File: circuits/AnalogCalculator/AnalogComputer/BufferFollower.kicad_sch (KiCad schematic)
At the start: 1 part, among them U7 LM324

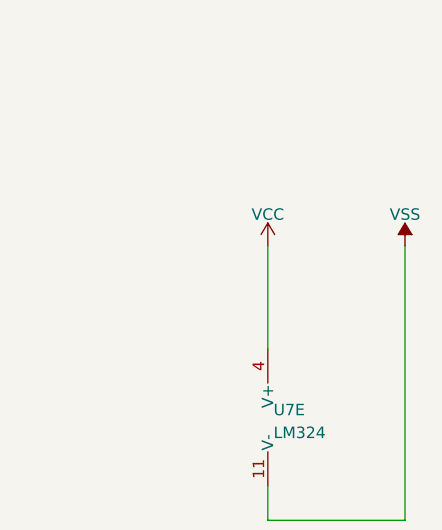
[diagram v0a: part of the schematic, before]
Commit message: update analog computer layout
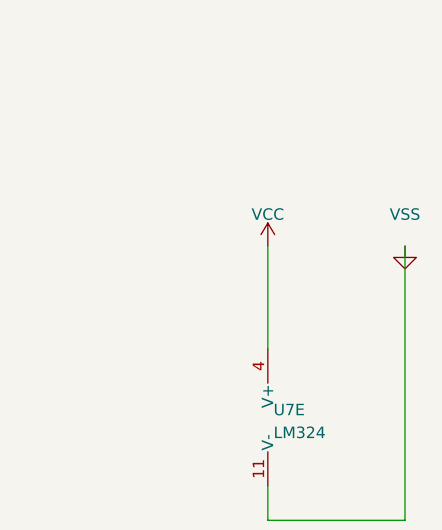
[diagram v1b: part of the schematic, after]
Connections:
- net VSS renamed GND
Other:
- company: (none) -> Out-of-band Development, LLC
- title: (none) -> Analog Computer
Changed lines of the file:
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@@
 (kicad_sch (version 20230121) (generator eeschema)
   (paper "A4")
+  (title_block
+    (title "Analog Computer")
+    (date "2023-03-08")
+    (rev "v1")
+    (company "Out-of-band Development, LLC")
+    (comment 1 "Matthew Whited")
+    (comment 2 "Buffer/Follower Amplifier")
+  )
   (junction (at 67.31 35.56) (diameter 0) (color 0 0 0 0)
   )
@@
     )
   )
-  (symbol (lib_id "power:VSS") (at 205.74 50.8 0) (unit 1)
+  (symbol (lib_id "power:GND") (at 205.74 50.8 0) (unit 1)
     (in_bom yes) (on_board yes) (dnp no) (fields_autoplaced)
     (property "Reference" "#PWR023" (at 205.74 54.61 0)

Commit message: update design
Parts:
- renumbered U7 to U12
